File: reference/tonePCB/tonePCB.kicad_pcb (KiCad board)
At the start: 2 copper layers, 39 x 62 mm, 13 parts, among them J1 to_ftdi, U1 ATMEGA328P-PU

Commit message: Adding power and ground copper pours
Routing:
- added copper zone on F.Cu, net +5V
- added copper zone on B.Cu, net Earth

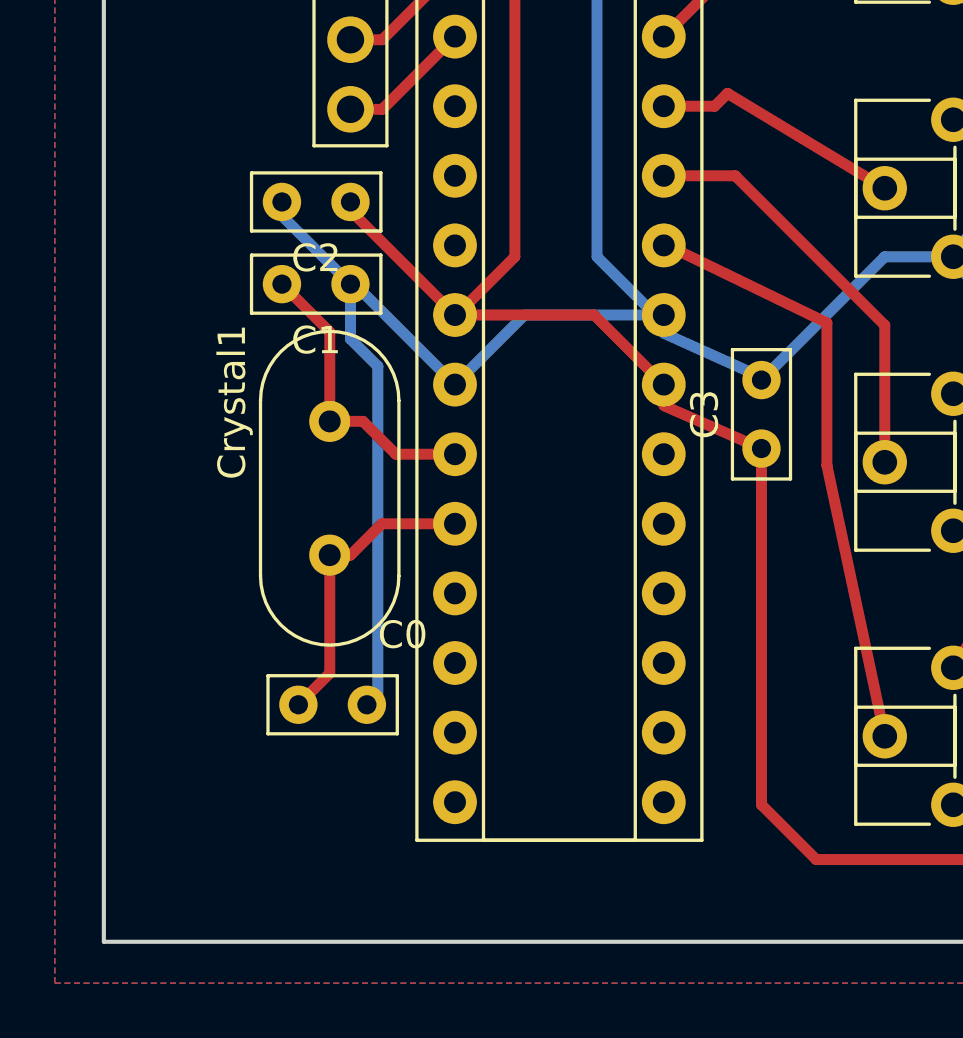
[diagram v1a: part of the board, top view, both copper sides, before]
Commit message: Adding an LED to the project
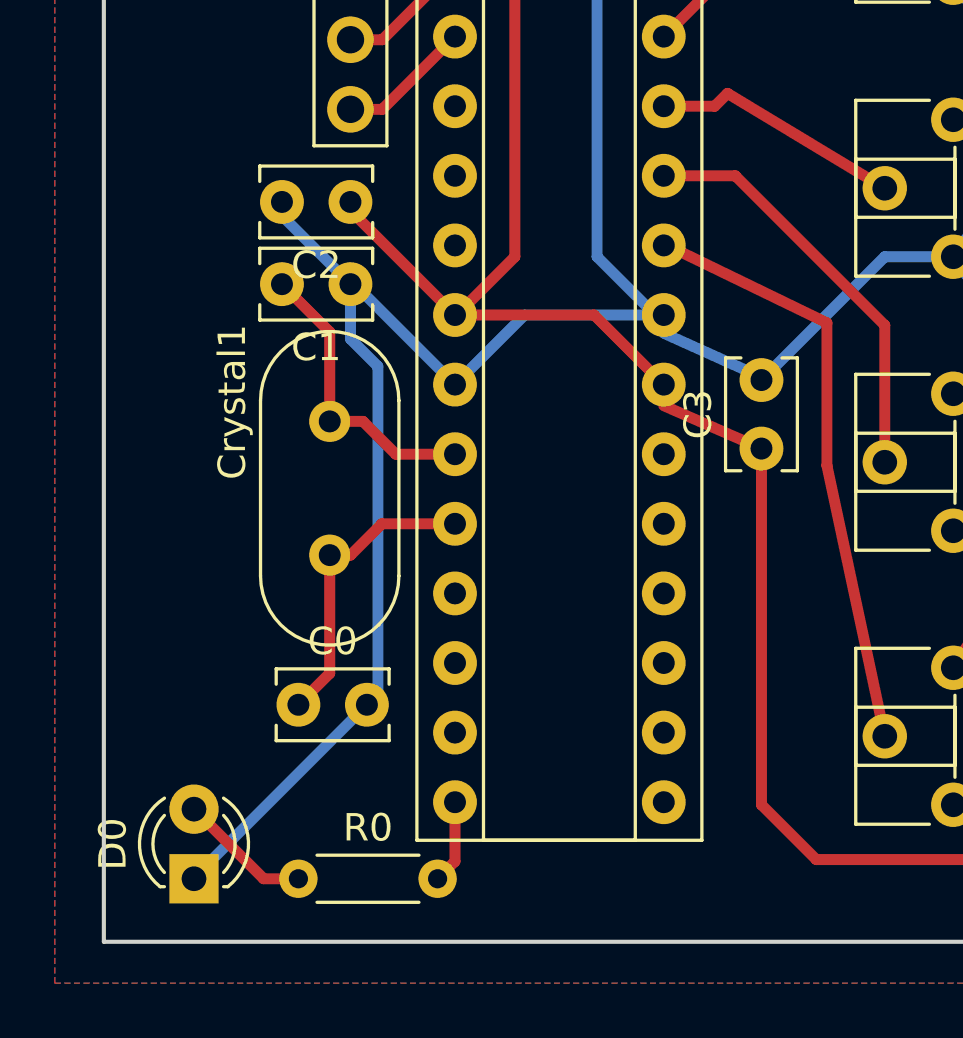
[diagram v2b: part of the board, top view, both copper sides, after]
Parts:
- added D0: LED, LEDs:LED_D3.0mm_FlatTop, F.Cu at (161.3, 139.7)
- added R0: 10K, Resistors_THT:R_Axial_DIN0204_L3.6mm_D1.6mm_P5.08mm_Horizontal, F.Cu at (165.1, 139.7)
- C0, C1, C2, C3: footprint Capacitors_THT:C_Rect_L4.6mm_W2.0mm_P2.50mm_MKS02_FKP02 -> Capacitors_THT:C_Rect_L4.0mm_W2.5mm_P2.50mm
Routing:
- net Earth: track 142.6 -> 151.6 mm
- net Net-(D0-Pad2): track 0.00 -> 4.86 mm
- net Net-(R0-Pad2): track 0.00 -> 3.06 mm

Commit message: Last commit before I try and refactor circuit
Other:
- board size 39 x 62 mm -> 40.6 x 66 mm
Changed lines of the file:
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@@
     (links 37)
     (no_connects 0)
-    (area 157.924999 79.924999 197.075001 142.075001)
+    (area 154.94 74.93 198.120001 144.780001)
     (thickness 1.6)
     (drawings 5)
@@
   (layers
     (0 F.Cu signal)
-    (31 B.Cu signal hide)
+    (31 B.Cu signal)
     (32 B.Adhes user)
     (33 F.Adhes user)
@@
   )
   (setup
-    (last_trace_width 0.4)
+    (last_trace_width 0.25)
     (user_trace_width 0.4)
     (trace_clearance 0.2)
@@
     (visible_elements FFFFFF7F)
     (pcbplotparams
-      (layerselection 0x00030_80000001)
+      (layerselection 0x00000_80000001)
       (usegerberextensions false)
       (excludeedgelayer true)
@@
       (padsonsilk false)
       (subtractmaskfromsilk false)
-      (outputformat 4)
+      (outputformat 5)
       (mirror false)
       (drillshape 0)
@@
     )
   )
-  (gr_line (start 158 104) (end 158 142) (angle 90) (layer Edge.Cuts) (width 0.15))
-  (gr_line (start 182 80) (end 158 104) (angle 90) (layer Edge.Cuts) (width 0.15))
-  (gr_line (start 197 80) (end 182 80) (angle 90) (layer Edge.Cuts) (width 0.15))
-  (gr_line (start 197 142) (end 197 80) (angle 90) (layer Edge.Cuts) (width 0.15))
-  (gr_line (start 158 142) (end 197 142) (angle 90) (layer Edge.Cuts) (width 0.15))
+  (gr_line (start 156.21 104.14) (end 156.21 143.51) (angle 90) (layer Edge.Cuts) (width 0.15))
+  (gr_line (start 182.88 77.47) (end 156.21 104.14) (angle 90) (layer Edge.Cuts) (width 0.15))
+  (gr_line (start 196.85 77.47) (end 182.88 77.47) (angle 90) (layer Edge.Cuts) (width 0.15))
+  (gr_line (start 196.85 143.51) (end 196.85 77.47) (angle 90) (layer Edge.Cuts) (width 0.15))
+  (gr_line (start 156.21 143.51) (end 196.85 143.51) (angle 90) (layer Edge.Cuts) (width 0.15))
   (segment (start 166.243 127.889) (end 166.243 132.207) (width 0.4) (layer F.Cu) (net 1))
   (segment (start 166.243 132.207) (end 165.1 133.35) (width 0.4) (layer F.Cu) (net 1))
@@
     (polygon
       (pts
-        (xy 198.12 143.51) (xy 156.21 143.51) (xy 156.21 78.74) (xy 198.12 78.74)
+        (xy 198.12 144.78) (xy 154.94 144.78) (xy 154.94 74.93) (xy 198.12 74.93)
       )
     )
@@
     (polygon
       (pts
-        (xy 198.12 143.51) (xy 156.21 143.51) (xy 156.21 78.74) (xy 198.12 78.74)
+        (xy 198.12 144.78) (xy 154.94 144.78) (xy 154.94 74.93) (xy 198.12 74.93)
       )
     )

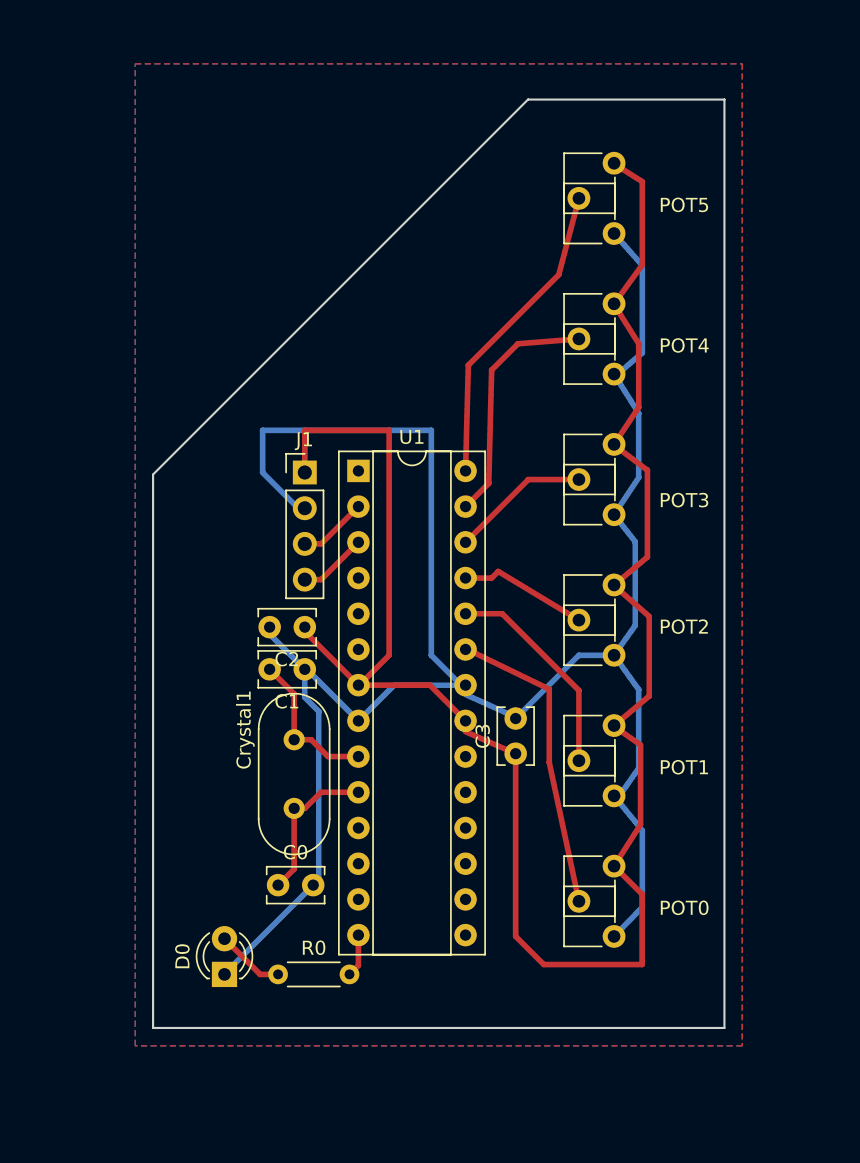
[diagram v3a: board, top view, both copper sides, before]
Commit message: Removing the back copper and the ground wiring
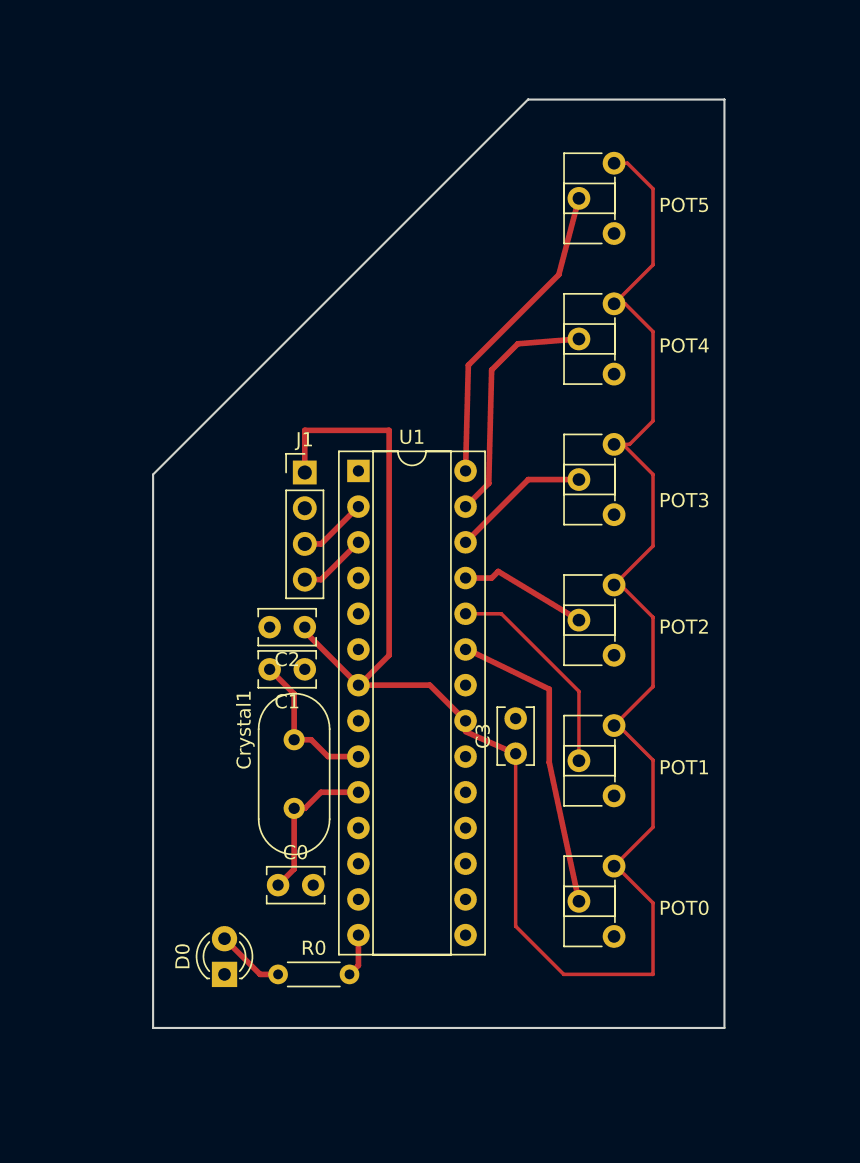
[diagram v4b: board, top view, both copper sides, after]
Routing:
- net Earth: track 151.6 -> 3.32 mm
- net +5V: track 136.7 -> 143.7 mm
- removed copper zone on F.Cu, net +5V
- removed copper zone on B.Cu, net Earth

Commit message: Replaced the ground traces with a copper pour
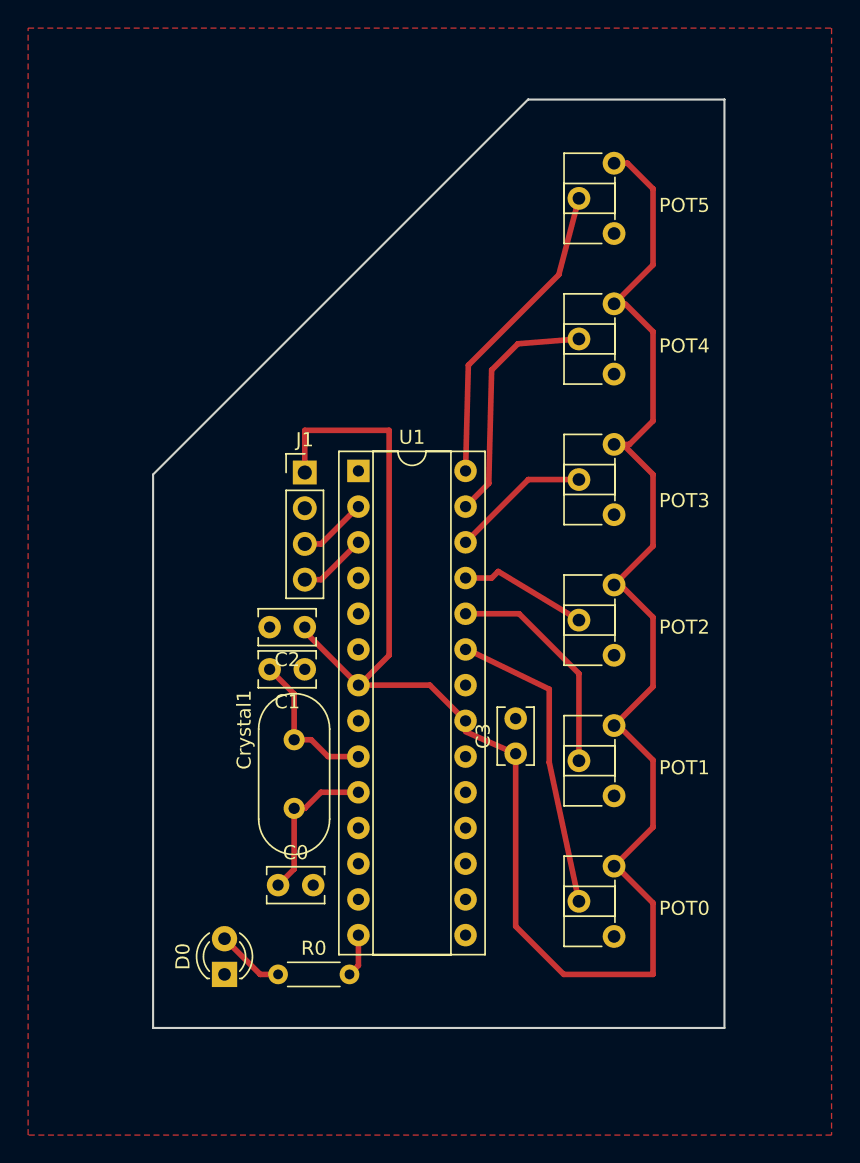
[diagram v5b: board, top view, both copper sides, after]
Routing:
- net Net-(POT1-Pad2): track 15.3 -> 16.0 mm
- added copper zone on F.Cu, net Earth
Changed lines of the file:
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@@
   (general
     (links 37)
-    (no_connects 13)
+    (no_connects 0)
     (area 154.94 74.93 198.120001 144.780001)
     (thickness 1.6)
@@
   )
   (setup
-    (last_trace_width 0.25)
+    (last_trace_width 0.4)
     (user_trace_width 0.4)
     (trace_clearance 0.2)
@@
   (segment (start 167.459 123.009) (end 168.656 124.206) (width 0.4) (layer F.Cu) (net 3))
   (segment (start 168.656 124.206) (end 170.815 124.206) (width 0.4) (layer F.Cu) (net 3))
-  (segment (start 189 132) (end 189.15 132) (width 0.25) (layer F.Cu) (net 4) (status C00000))
-  (segment (start 189.15 132) (end 191.77 134.62) (width 0.25) (layer F.Cu) (net 4) (status 400000))
-  (segment (start 182 136.28) (end 182 124) (width 0.25) (layer F.Cu) (net 4) (status 800000))
-  (segment (start 185.42 139.7) (end 182 136.28) (width 0.25) (layer F.Cu) (net 4))
-  (segment (start 191.77 139.7) (end 185.42 139.7) (width 0.25) (layer F.Cu) (net 4))
-  (segment (start 191.77 134.62) (end 191.77 139.7) (width 0.25) (layer F.Cu) (net 4))
-  (segment (start 189 122) (end 189.31 122) (width 0.25) (layer F.Cu) (net 4) (status C00000))
-  (segment (start 189.31 122) (end 191.77 124.46) (width 0.25) (layer F.Cu) (net 4) (status 400000))
-  (segment (start 191.77 129.23) (end 189 132) (width 0.25) (layer F.Cu) (net 4) (status 800000))
-  (segment (start 191.77 124.46) (end 191.77 129.23) (width 0.25) (layer F.Cu) (net 4))
+  (segment (start 182 136.28) (end 182 124) (width 0.4) (layer F.Cu) (net 4))
+  (segment (start 189.15 132) (end 191.77 134.62) (width 0.4) (layer F.Cu) (net 4))
+  (segment (start 191.77 134.62) (end 191.77 139.7) (width 0.4) (layer F.Cu) (net 4))
+  (segment (start 191.77 139.7) (end 185.42 139.7) (width 0.4) (layer F.Cu) (net 4))
+  (segment (start 185.42 139.7) (end 182 136.28) (width 0.4) (layer F.Cu) (net 4))
+  (segment (start 189 132) (end 189.15 132) (width 0.25) (layer F.Cu) (net 4))
+  (segment (start 189 122) (end 189.31 122) (width 0.25) (layer F.Cu) (net 4))
+  (segment (start 189.31 122) (end 191.77 124.46) (width 0.4) (layer F.Cu) (net 4))
+  (segment (start 191.77 124.46) (end 191.77 129.23) (width 0.4) (layer F.Cu) (net 4))
+  (segment (start 191.77 129.23) (end 189 132) (width 0.4) (layer F.Cu) (net 4))
   (segment (start 189 112) (end 189.47 112) (width 0.25) (layer F.Cu) (net 4))
-  (segment (start 189.47 112) (end 191.77 114.3) (width 0.25) (layer F.Cu) (net 4))
-  (segment (start 191.77 119.23) (end 189 122) (width 0.25) (layer F.Cu) (net 4))
-  (segment (start 191.77 114.3) (end 191.77 119.23) (width 0.25) (layer F.Cu) (net 4))
+  (segment (start 189.47 112) (end 191.77 114.3) (width 0.4) (layer F.Cu) (net 4))
+  (segment (start 191.77 114.3) (end 191.77 119.23) (width 0.4) (layer F.Cu) (net 4))
+  (segment (start 191.77 119.23) (end 189 122) (width 0.4) (layer F.Cu) (net 4))
   (segment (start 189 102) (end 189.63 102) (width 0.25) (layer F.Cu) (net 4))
-  (segment (start 189.63 102) (end 191.77 104.14) (width 0.25) (layer F.Cu) (net 4))
-  (segment (start 191.77 109.23) (end 189 112) (width 0.25) (layer F.Cu) (net 4))
-  (segment (start 191.77 104.14) (end 191.77 109.23) (width 0.25) (layer F.Cu) (net 4))
-  (segment (start 189 102) (end 190.1 102) (width 0.25) (layer F.Cu) (net 4))
-  (segment (start 191.77 93.98) (end 191.77 100.33) (width 0.25) (layer F.Cu) (net 4))
-  (segment (start 191.77 93.98) (end 189.79 92) (width 0.25) (layer F.Cu) (net 4))
-  (segment (start 190.1 102) (end 191.77 100.33) (width 0.25) (layer F.Cu) (net 4))
+  (segment (start 189.63 102) (end 191.77 104.14) (width 0.4) (layer F.Cu) (net 4))
+  (segment (start 191.77 104.14) (end 191.77 109.23) (width 0.4) (layer F.Cu) (net 4))
+  (segment (start 191.77 109.23) (end 189 112) (width 0.4) (layer F.Cu) (net 4))
+  (segment (start 189 102) (end 190.1 102) (width 0.4) (layer F.Cu) (net 4))
+  (segment (start 190.1 102) (end 191.77 100.33) (width 0.4) (layer F.Cu) (net 4))
+  (segment (start 191.77 93.98) (end 189.79 92) (width 0.4) (layer F.Cu) (net 4))
+  (segment (start 191.77 93.98) (end 191.77 100.33) (width 0.4) (layer F.Cu) (net 4))
   (segment (start 189 92) (end 189.79 92) (width 0.25) (layer F.Cu) (net 4))
-  (segment (start 189 82) (end 189.95 82) (width 0.25) (layer F.Cu) (net 4))
-  (segment (start 191.77 89.23) (end 189 92) (width 0.25) (layer F.Cu) (net 4))
-  (segment (start 191.77 83.82) (end 191.77 89.23) (width 0.25) (layer F.Cu) (net 4))
-  (segment (start 189.95 82) (end 191.77 83.82) (width 0.25) (layer F.Cu) (net 4))
+  (segment (start 189 82) (end 189.95 82) (width 0.4) (layer F.Cu) (net 4))
+  (segment (start 189.95 82) (end 191.77 83.82) (width 0.4) (layer F.Cu) (net 4))
+  (segment (start 191.77 83.82) (end 191.77 89.23) (width 0.4) (layer F.Cu) (net 4))
+  (segment (start 191.77 89.23) (end 189 92) (width 0.4) (layer F.Cu) (net 4))
   (segment (start 167 104) (end 167 101) (width 0.4) (layer F.Cu) (net 4))
   (segment (start 167 101) (end 173 101) (width 0.4) (layer F.Cu) (net 4))
@@
   (segment (start 184.388 124.619) (end 186.5 134.5) (width 0.4) (layer F.Cu) (net 5) (status 20))
   (segment (start 184.388 119.412) (end 184.388 124.619) (width 0.4) (layer F.Cu) (net 5))
-  (segment (start 186.5 124.5) (end 186.5 119.57) (width 0.25) (layer F.Cu) (net 6) (status 400000))
-  (segment (start 180.976 114.046) (end 178.435 114.046) (width 0.25) (layer F.Cu) (net 6) (status 800000))
-  (segment (start 186.5 119.57) (end 180.976 114.046) (width 0.25) (layer F.Cu) (net 6))
+  (segment (start 186.5 124.5) (end 186.5 118.3) (width 0.4) (layer F.Cu) (net 6))
+  (segment (start 182.246 114.046) (end 178.435 114.046) (width 0.4) (layer F.Cu) (net 6))
+  (segment (start 186.5 118.3) (end 182.246 114.046) (width 0.4) (layer F.Cu) (net 6))
   (segment (start 186.5 114.5) (end 180.761 111.038) (width 0.4) (layer F.Cu) (net 7) (status 10))
   (segment (start 180.761 111.038) (end 180.293 111.506) (width 0.4) (layer F.Cu) (net 7))
@@
   (segment (start 170.815 136.906) (end 170.815 139.065) (width 0.4) (layer F.Cu) (net 27))
   (segment (start 170.815 139.065) (end 170.18 139.7) (width 0.4) (layer F.Cu) (net 27))
+  (zone (net 2) (net_name Earth) (layer F.Cu) (hatch edge 0.508)
+    (connect_pads (clearance 0.508))
+    (min_thickness 0.254)
+    (fill yes (arc_segments 16) (thermal_gap 0.508) (thermal_bridge_width 0.508))
+    (polygon
+      (pts
+        (xy 204.47 151.13) (xy 147.32 151.13) (xy 147.32 72.39) (xy 204.47 72.39)
+      )
+    )
+  )
 )
